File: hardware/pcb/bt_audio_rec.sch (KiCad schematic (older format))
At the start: 62 parts, among them IC1 RN52-I_RM116, IC2 VCNL4200, J1 OutL, J13 Power, J14 PROX Socket, J15 PROX Header, J2 Conn_01x31, J3 RN52 factory reset, J4 ERM, J5 OutR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

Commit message: Update proximity cap value, upate PCB notes.
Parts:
- C12: value 2.2uF -> 4.7uF
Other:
- note added: "RdsOn(3.3Vgs) = 0.18R@125degC\ndissipation@500mA = 0.18 * 0.5 * 0.5 = 45mW\n"
- note removed: "RdsOn(3.3Vgs) = 0.18R@125degC\ndissipation@500mA = 0.18 * 0.5 * 0.5 = 16mW\n"
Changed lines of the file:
@@
 P 10500 7700
 F 0 "C12" H 10615 7746 50  0000 L CNN
-F 1 "2.2uF" H 10615 7655 50  0000 L CNN
+F 1 "4.7uF" H 10615 7655 50  0000 L CNN
 F 2 "Capacitor_SMD:C_0603_1608Metric" H 10538 7550 50  0001 C CNN
 F 3 "~" H 10500 7700 50  0001 C CNN
@@
 PROX_I2C_SCK
 Text Notes 3000 7850 0    50   ~ 0
-RdsOn(3.3Vgs) = 0.18R@125degC\ndissipation@500mA = 0.18 * 0.5 * 0.5 = 16mW\n
+RdsOn(3.3Vgs) = 0.18R@125degC\ndissipation@500mA = 0.18 * 0.5 * 0.5 = 45mW\n
 Wire Wire Line
 	12900 3350 13050 3350

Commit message: Fix GPIO4 tied low and backwards MOSFET error
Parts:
- removed R9: 10k, Resistor_SMD:R_0603_1608Metric, symbol Device:R
- J3: footprint Connector_PinHeader_2.54mm:PinHeader_1x02_P2.54mm_Horizontal -> Connector_PinHeader_2.54mm:PinHeader_1x03_P2.54mm_Horizontal; symbol Connector:Conn_01x02_Male -> Connector:Conn_01x03_Male
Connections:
- net GND: now also J3.3 (Pin_3)
- net LED+: now also Q4.3 (D); no longer Q4.2 (S)
- net PROX_3.3V: now also Q4.2 (S); no longer Q4.3 (D)
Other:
- note added: "(Viref - Vss) / Iref\nIref = 15.625μA\n= 515k@8.04V"
- note removed: "(Viref - Vss) / Iref\nIref = 15.625μA\n= 569k@8.9V"
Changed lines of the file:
@@
 GPIO_OUT_DISP_CMD
 $Comp
-L Connector:Conn_01x02_Male J3
+L Connector:Conn_01x03_Male J3
 U 1 1 5EB3C69A
-P 2550 5000
-F 0 "J3" H 2800 5250 50  0000 C CNN
-F 1 "RN52 factory reset" H 2800 5150 50  0000 C CNN
-F 2 "Connector_PinHeader_2.54mm:PinHeader_1x02_P2.54mm_Horizontal" H 2550 5000 50  0001 C CNN
-F 3 "~" H 2550 5000 50  0001 C CNN
-	1    2550 5000
+P 2550 5100
+F 0 "J3" H 2800 5450 50  0000 C CNN
+F 1 "RN52 factory reset" H 2800 5350 50  0000 C CNN
+F 2 "Connector_PinHeader_2.54mm:PinHeader_1x03_P2.54mm_Horizontal" H 2550 5100 50  0001 C CNN
+F 3 "~" H 2550 5100 50  0001 C CNN
+	1    2550 5100
 	1    0    0    -1
 $EndComp
@@
 Text GLabel 1500 1300 0    39   Input ~ 0
 RN52_EVENT
-$Comp
-L power:GND #PWR0109
-U 1 1 5EB44A53
-P 2800 5550
-F 0 "#PWR0109" H 2800 5300 50  0001 C CNN
-F 1 "GND" H 2805 5377 50  0000 C CNN
-F 2 "" H 2800 5550 50  0001 C CNN
-F 3 "" H 2800 5550 50  0001 C CNN
-	1    2800 5550
-	1    0    0    -1
-$EndComp
-$Comp
-L Device:R R9
-U 1 1 5EB460F9
-P 2800 5350
-F 0 "R9" H 2870 5396 50  0000 L CNN
-F 1 "10k" H 2870 5305 50  0000 L CNN
-F 2 "Resistor_SMD:R_0603_1608Metric" V 2730 5350 50  0001 C CNN
-F 3 "~" H 2800 5350 50  0001 C CNN
-	1    2800 5350
-	1    0    0    -1
-$EndComp
 Wire Wire Line
 	2750 5000 2900 5000
@@
 U 1 1 5ED5A120
 P 10000 7950
-F 0 "Q4" H 9800 7850 50  0000 L CNN
-F 1 "DMG2301L" H 9650 7750 50  0000 L CNN
+F 0 "Q4" H 9800 8050 50  0000 L CNN
+F 1 "DMG2301L" H 9650 8150 50  0000 L CNN
 F 2 "Package_TO_SOT_SMD:SOT-23" H 10200 7875 50  0001 L CIN
 F 3 "https://www.diodes.com/assets/Datasheets/DMG2301L.pdf" H 10000 7950 50  0001 L CNN
 	1    10000 7950
-	1    0    0    -1
+	1    0    0    1
 $EndComp
 $Comp
@@
 256x64 4-bit Display\nSH1122\n- 8-bit 8080\n- 8-bit 6800\n- 3/4-wire SPI\n
 Text Notes 12850 5450 0    50   ~ 0
-(Viref - Vss) / Iref\nIref = 15.625μA\n= 569k@8.9V
+(Viref - Vss) / Iref\nIref = 15.625μA\n= 515k@8.04V
 Text Notes 3600 9400 0    50   ~ 0
 Haptic Feedback
@@
 	1    0    0    -1
 $EndComp
-Wire Wire Line
-	2800 5500 2800 5550
-Wire Wire Line
-	2750 5100 2800 5100
-Wire Wire Line
-	2800 5200 2800 5100
-Connection ~ 2800 5100
-Wire Wire Line
-	2800 5100 2900 5100
 $Comp
 L power:GND #PWR0103
@@
 Text GLabel 1500 2100 0    39   Input ~ 0
 RN52_CMD_MODE
+Wire Wire Line
+	2750 5100 2900 5100
+$Comp
+L power:GND #PWR0109
+U 1 1 5F6C17CF
+P 2750 5200
+F 0 "#PWR0109" H 2750 4950 50  0001 C CNN
+F 1 "GND" H 2755 5027 50  0000 C CNN
+F 2 "" H 2750 5200 50  0001 C CNN
+F 3 "" H 2750 5200 50  0001 C CNN
+	1    2750 5200
+	1    0    0    -1
+$EndComp
 $EndSCHEMATC

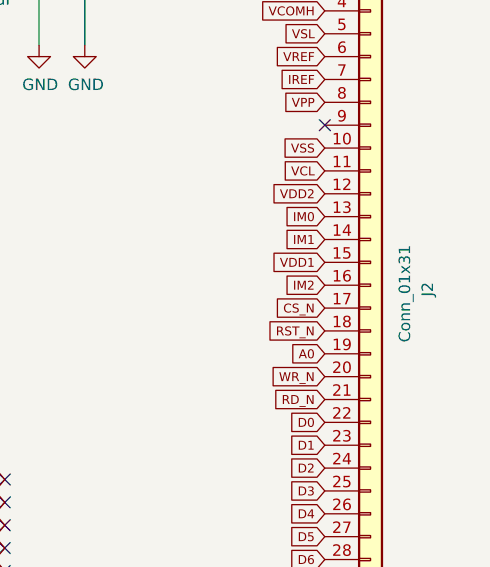
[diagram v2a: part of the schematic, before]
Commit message: Update connector label
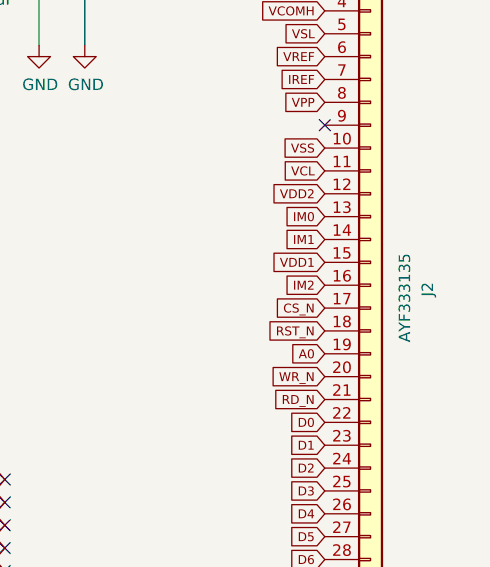
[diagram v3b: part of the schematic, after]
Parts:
- J2: value Conn_01x31 -> AYF333135
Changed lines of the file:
@@
 P 15100 7350
 F 0 "J2" V 15350 7300 50  0000 L CNN
-F 1 "Conn_01x31" V 15250 7100 50  0000 L CNN
+F 1 "AYF333135" V 15250 7100 50  0000 L CNN
 F 2 "BOB_General:FPC_Socket_0.3_31_Panasonic_AYF333135" H 15100 7350 50  0001 C CNN
 F 3 "~" H 15100 7350 50  0001 C CNN
